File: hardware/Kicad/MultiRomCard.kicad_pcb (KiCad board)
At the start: 2 copper layers, 160 x 100 mm, 17 parts, among them P1 VC4000_Cartridge_Bus, P2 MicroSD_Breakout, U1 Arduino_UNO, U2 74HC595, U3 74HC595, U4 74HC595, U5 6264, U6 74HC245, U7 74HC245, U8 74HC245

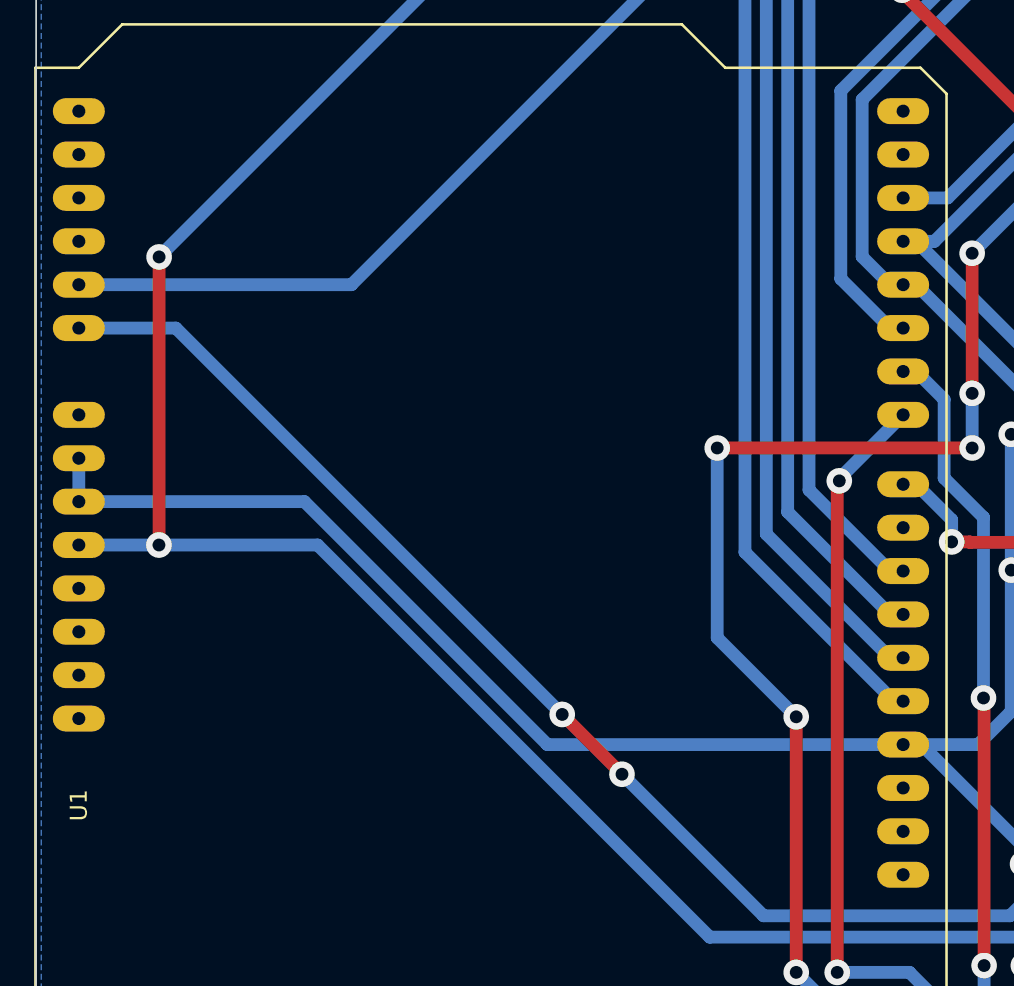
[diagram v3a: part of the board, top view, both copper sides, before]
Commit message: [PCB] Slightly bigger drill holes for Arduino footprint.
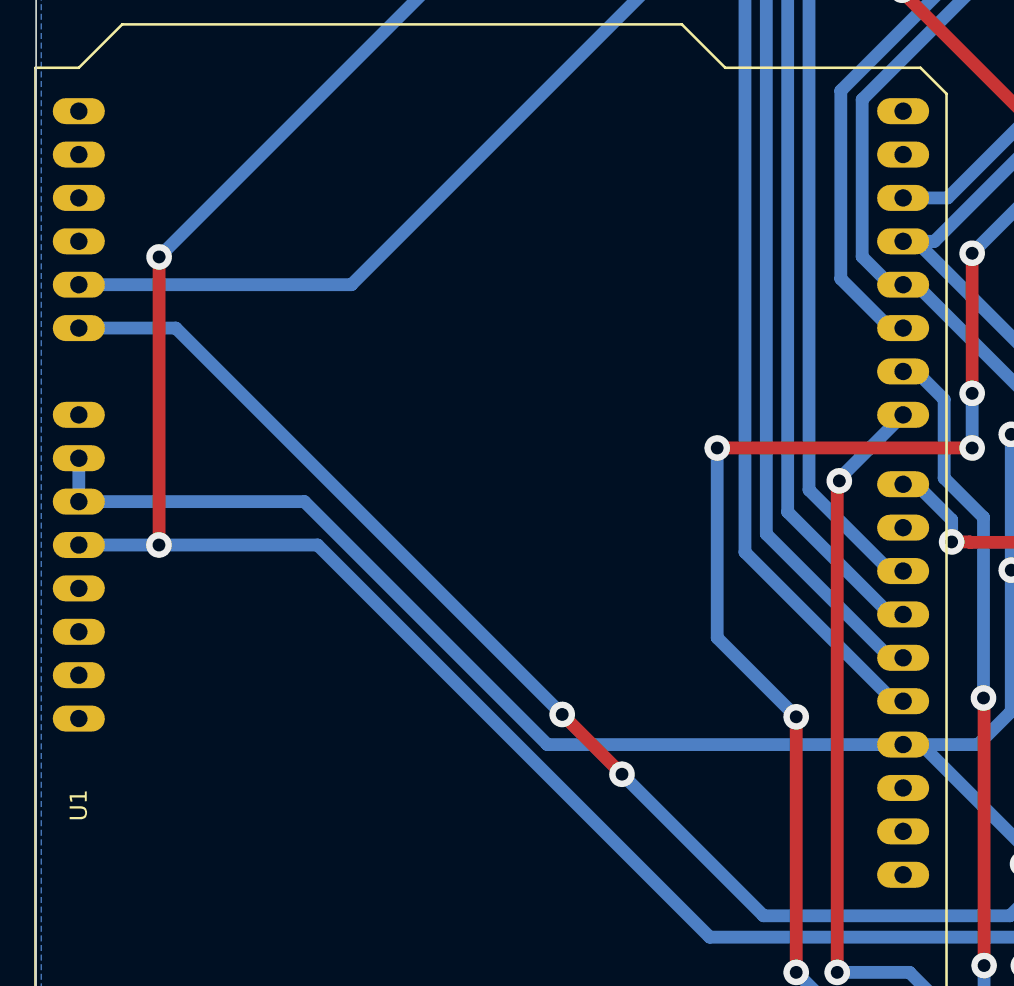
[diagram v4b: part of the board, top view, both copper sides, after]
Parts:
- U1: footprint VC4000_MultiRom:Arduino_UNO -> Arduino_UNO
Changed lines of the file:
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@@
-(kicad_pcb (version 4) (host pcbnew "(2015-06-18 BZR 5783)-product")
+(kicad_pcb (version 4) (host pcbnew "(2015-06-22 BZR 5801)-product")
   (general
     (links 133)
@@
     (uvia_drill 0.127)
   )
-  (module VC4000_MultiRom:Arduino_UNO (layer F.Cu)
+  (module Arduino_UNO (layer F.Cu)
     (at 93.9 118 270)
     (fp_text reference U1 (at 7.62 25.4 270) (layer F.SilkS)
@@
     (fp_line (start 30.48 24.765) (end 32.385 24.765) (layer F.SilkS) (width 0.15))
     (fp_line (start 30.48 27.94) (end 30.48 24.765) (layer F.SilkS) (width 0.15))
-    (pad 18 thru_hole oval (at 11.684 -22.86 270) (size 1.524 3.048) (drill 0.762) (layers *.Cu *.Mask F.SilkS))
-    (pad 17 thru_hole oval (at 9.144 -22.86 270) (size 1.524 3.048) (drill 0.762) (layers *.Cu *.Mask F.SilkS))
-    (pad 16 thru_hole oval (at 6.604 -22.86 270) (size 1.524 3.048) (drill 0.762) (layers *.Cu *.Mask F.SilkS)
+    (pad 18 thru_hole oval (at 11.684 -22.86 270) (size 1.524 3.048) (drill 1.016) (layers *.Cu *.Mask F.SilkS))
+    (pad 17 thru_hole oval (at 9.144 -22.86 270) (size 1.524 3.048) (drill 1.016) (layers *.Cu *.Mask F.SilkS))
+    (pad 16 thru_hole oval (at 6.604 -22.86 270) (size 1.524 3.048) (drill 1.016) (layers *.Cu *.Mask F.SilkS)
       (net 29 "Net-(U1-Pad16)"))
-    (pad 15 thru_hole oval (at 4.064 -22.86 270) (size 1.524 3.048) (drill 0.762) (layers *.Cu *.Mask F.SilkS)
+    (pad 15 thru_hole oval (at 4.064 -22.86 270) (size 1.524 3.048) (drill 1.016) (layers *.Cu *.Mask F.SilkS)
       (net 25 GND))
-    (pad 14 thru_hole oval (at 1.524 -22.86 270) (size 1.524 3.048) (drill 0.762) (layers *.Cu *.Mask F.SilkS)
+    (pad 14 thru_hole oval (at 1.524 -22.86 270) (size 1.524 3.048) (drill 1.016) (layers *.Cu *.Mask F.SilkS)
       (net 80 "Net-(P2-Pad1)"))
-    (pad 13 thru_hole oval (at -1.016 -22.86 270) (size 1.524 3.048) (drill 0.762) (layers *.Cu *.Mask F.SilkS)
+    (pad 13 thru_hole oval (at -1.016 -22.86 270) (size 1.524 3.048) (drill 1.016) (layers *.Cu *.Mask F.SilkS)
       (net 81 "Net-(P2-Pad2)"))
-    (pad 12 thru_hole oval (at -3.556 -22.86 270) (size 1.524 3.048) (drill 0.762) (layers *.Cu *.Mask F.SilkS)
+    (pad 12 thru_hole oval (at -3.556 -22.86 270) (size 1.524 3.048) (drill 1.016) (layers *.Cu *.Mask F.SilkS)
       (net 82 "Net-(P2-Pad3)"))
-    (pad 11 thru_hole oval (at -6.096 -22.86 270) (size 1.524 3.048) (drill 0.762) (layers *.Cu *.Mask F.SilkS)
+    (pad 11 thru_hole oval (at -6.096 -22.86 270) (size 1.524 3.048) (drill 1.016) (layers *.Cu *.Mask F.SilkS)
       (net 83 "Net-(P2-Pad4)"))
-    (pad 10 thru_hole oval (at -8.636 -22.86 270) (size 1.524 3.048) (drill 0.762) (layers *.Cu *.Mask F.SilkS)
+    (pad 10 thru_hole oval (at -8.636 -22.86 270) (size 1.524 3.048) (drill 1.016) (layers *.Cu *.Mask F.SilkS)
       (net 30 "Net-(U1-Pad10)"))
-    (pad 9 thru_hole oval (at -11.176 -22.86 270) (size 1.524 3.048) (drill 0.762) (layers *.Cu *.Mask F.SilkS)
+    (pad 9 thru_hole oval (at -11.176 -22.86 270) (size 1.524 3.048) (drill 1.016) (layers *.Cu *.Mask F.SilkS)
       (net 31 CE2SRAM))
-    (pad 8 thru_hole oval (at -15.24 -22.86 270) (size 1.524 3.048) (drill 0.762) (layers *.Cu *.Mask F.SilkS)
+    (pad 8 thru_hole oval (at -15.24 -22.86 270) (size 1.524 3.048) (drill 1.016) (layers *.Cu *.Mask F.SilkS)
       (net 32 CE1SRAM))
-    (pad 7 thru_hole oval (at -17.78 -22.86 270) (size 1.524 3.048) (drill 0.762) (layers *.Cu *.Mask F.SilkS)
+    (pad 7 thru_hole oval (at -17.78 -22.86 270) (size 1.524 3.048) (drill 1.016) (layers *.Cu *.Mask F.SilkS)
       (net 33 OEVCBUS))
-    (pad 6 thru_hole oval (at -20.32 -22.86 270) (size 1.524 3.048) (drill 0.762) (layers *.Cu *.Mask F.SilkS)
+    (pad 6 thru_hole oval (at -20.32 -22.86 270) (size 1.524 3.048) (drill 1.016) (layers *.Cu *.Mask F.SilkS)
       (net 34 "Net-(U1-Pad6)"))
-    (pad 5 thru_hole oval (at -22.86 -22.86 270) (size 1.524 3.048) (drill 0.762) (layers *.Cu *.Mask F.SilkS)
+    (pad 5 thru_hole oval (at -22.86 -22.86 270) (size 1.524 3.048) (drill 1.016) (layers *.Cu *.Mask F.SilkS)
       (net 35 "Net-(U1-Pad5)"))
-    (pad 4 thru_hole oval (at -25.4 -22.86 270) (size 1.524 3.048) (drill 0.762) (layers *.Cu *.Mask F.SilkS)
+    (pad 4 thru_hole oval (at -25.4 -22.86 270) (size 1.524 3.048) (drill 1.016) (layers *.Cu *.Mask F.SilkS)
       (net 36 "Net-(U1-Pad4)"))
-    (pad 3 thru_hole oval (at -27.94 -22.86 270) (size 1.524 3.048) (drill 0.762) (layers *.Cu *.Mask F.SilkS)
+    (pad 3 thru_hole oval (at -27.94 -22.86 270) (size 1.524 3.048) (drill 1.016) (layers *.Cu *.Mask F.SilkS)
       (net 37 WESRAM))
-    (pad 2 thru_hole oval (at -30.48 -22.86 270) (size 1.524 3.048) (drill 0.762) (layers *.Cu *.Mask F.SilkS)
+    (pad 2 thru_hole oval (at -30.48 -22.86 270) (size 1.524 3.048) (drill 1.016) (layers *.Cu *.Mask F.SilkS)
       (net 38 "Net-(U1-Pad2)"))
-    (pad 1 thru_hole oval (at -33.02 -22.86 270) (size 1.524 3.048) (drill 0.762) (layers *.Cu *.Mask F.SilkS)
+    (pad 1 thru_hole oval (at -33.02 -22.86 270) (size 1.524 3.048) (drill 1.016) (layers *.Cu *.Mask F.SilkS)
       (net 39 "Net-(U1-Pad1)"))
-    (pad 32 thru_hole oval (at -33.02 25.4 270) (size 1.524 3.048) (drill 0.762) (layers *.Cu *.Mask F.SilkS)
+    (pad 32 thru_hole oval (at -33.02 25.4 270) (size 1.524 3.048) (drill 1.016) (layers *.Cu *.Mask F.SilkS)
       (net 40 "Net-(U1-Pad32)"))
-    (pad 31 thru_hole oval (at -30.48 25.4 270) (size 1.524 3.048) (drill 0.762) (layers *.Cu *.Mask F.SilkS)
+    (pad 31 thru_hole oval (at -30.48 25.4 270) (size 1.524 3.048) (drill 1.016) (layers *.Cu *.Mask F.SilkS)
       (net 41 "Net-(U1-Pad31)"))
-    (pad 30 thru_hole oval (at -27.94 25.4 270) (size 1.524 3.048) (drill 0.762) (layers *.Cu *.Mask F.SilkS)
+    (pad 30 thru_hole oval (at -27.94 25.4 270) (size 1.524 3.048) (drill 1.016) (layers *.Cu *.Mask F.SilkS)
       (net 42 "Net-(U1-Pad30)"))
-    (pad 29 thru_hole oval (at -25.4 25.4 270) (size 1.524 3.048) (drill 0.762) (layers *.Cu *.Mask F.SilkS)
+    (pad 29 thru_hole oval (at -25.4 25.4 270) (size 1.524 3.048) (drill 1.016) (layers *.Cu *.Mask F.SilkS)
       (net 43 "Net-(U1-Pad29)"))
-    (pad 28 thru_hole oval (at -22.86 25.4 270) (size 1.524 3.048) (drill 0.762) (layers *.Cu *.Mask F.SilkS)
+    (pad 28 thru_hole oval (at -22.86 25.4 270) (size 1.524 3.048) (drill 1.016) (layers *.Cu *.Mask F.SilkS)
       (net 44 "Net-(U1-Pad28)"))
-    (pad 27 thru_hole oval (at -20.32 25.4 270) (size 1.524 3.048) (drill 0.762) (layers *.Cu *.Mask F.SilkS)
+    (pad 27 thru_hole oval (at -20.32 25.4 270) (size 1.524 3.048) (drill 1.016) (layers *.Cu *.Mask F.SilkS)
       (net 45 "Net-(U1-Pad27)"))
-    (pad 26 thru_hole oval (at -15.24 25.4 270) (size 1.524 3.048) (drill 0.762) (layers *.Cu *.Mask F.SilkS)
+    (pad 26 thru_hole oval (at -15.24 25.4 270) (size 1.524 3.048) (drill 1.016) (layers *.Cu *.Mask F.SilkS)
       (net 46 "Net-(U1-Pad26)"))
-    (pad 25 thru_hole oval (at -12.7 25.4 270) (size 1.524 3.048) (drill 0.762) (layers *.Cu *.Mask F.SilkS)
+    (pad 25 thru_hole oval (at -12.7 25.4 270) (size 1.524 3.048) (drill 1.016) (layers *.Cu *.Mask F.SilkS)
       (net 25 GND))
-    (pad 24 thru_hole oval (at -10.16 25.4 270) (size 1.524 3.048) (drill 0.762) (layers *.Cu *.Mask F.SilkS)
+    (pad 24 thru_hole oval (at -10.16 25.4 270) (size 1.524 3.048) (drill 1.016) (layers *.Cu *.Mask F.SilkS)
       (net 25 GND))
-    (pad 23 thru_hole oval (at -7.62 25.4 270) (size 1.524 3.048) (drill 0.762) (layers *.Cu *.Mask F.SilkS)
+    (pad 23 thru_hole oval (at -7.62 25.4 270) (size 1.524 3.048) (drill 1.016) (layers *.Cu *.Mask F.SilkS)
       (net 13 VCC))
-    (pad 22 thru_hole oval (at -5.08 25.4 270) (size 1.524 3.048) (drill 0.762) (layers *.Cu *.Mask F.SilkS)
+    (pad 22 thru_hole oval (at -5.08 25.4 270) (size 1.524 3.048) (drill 1.016) (layers *.Cu *.Mask F.SilkS)
       (net 47 "Net-(U1-Pad22)"))
-    (pad 21 thru_hole oval (at -2.54 25.4 270) (size 1.524 3.048) (drill 0.762) (layers *.Cu *.Mask F.SilkS)
+    (pad 21 thru_hole oval (at -2.54 25.4 270) (size 1.524 3.048) (drill 1.016) (layers *.Cu *.Mask F.SilkS)
       (net 48 "Net-(U1-Pad21)"))
-    (pad 20 thru_hole oval (at 0 25.4 270) (size 1.524 3.048) (drill 0.762) (layers *.Cu *.Mask F.SilkS)
+    (pad 20 thru_hole oval (at 0 25.4 270) (size 1.524 3.048) (drill 1.016) (layers *.Cu *.Mask F.SilkS)
       (net 49 "Net-(U1-Pad20)"))
-    (pad 19 thru_hole oval (at 2.54 25.4 270) (size 1.524 3.048) (drill 0.762) (layers *.Cu *.Mask F.SilkS))
+    (pad 19 thru_hole oval (at 2.54 25.4 270) (size 1.524 3.048) (drill 1.016) (layers *.Cu *.Mask F.SilkS))
   )
   (module Housings_DIP:DIP-16__300_ELL (layer F.Cu)

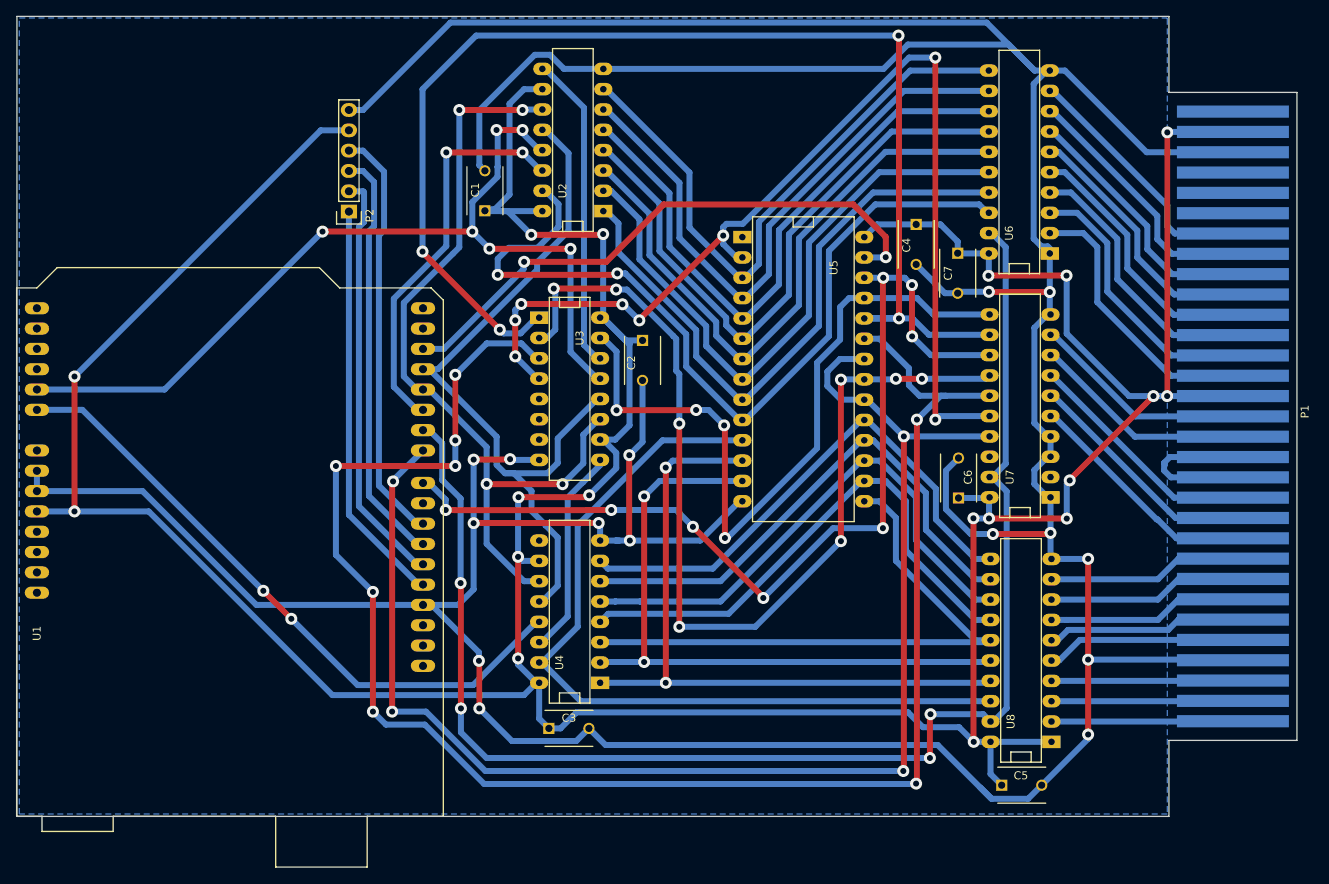
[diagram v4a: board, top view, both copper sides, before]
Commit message: [SCH/PCB] Replace Arduino UNO by Arduino Nano
- TODO: Shrink board outlines to account for smaller Arduino board.
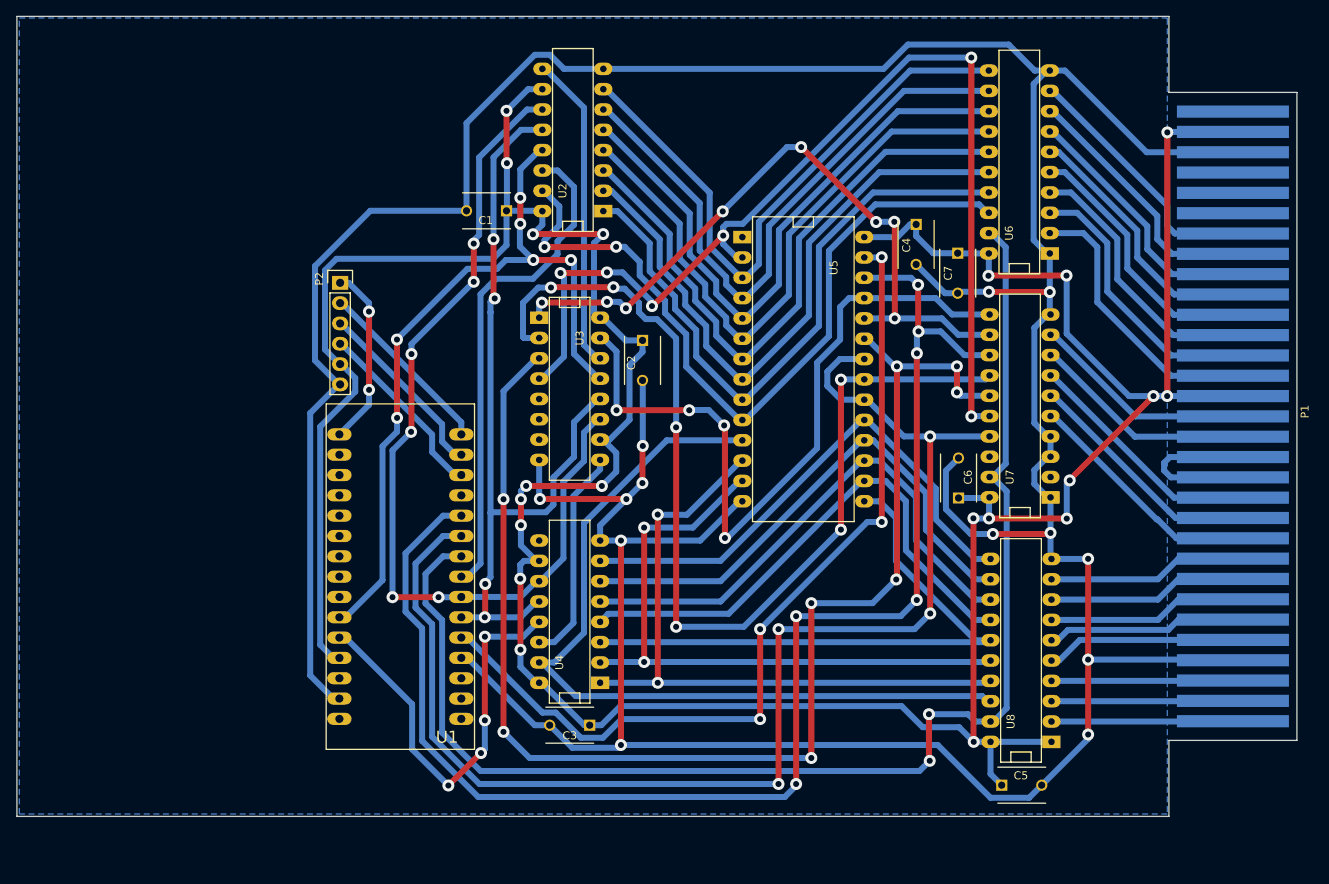
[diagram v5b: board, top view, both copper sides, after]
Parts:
- U1: value Arduino_UNO -> Arduino_Nano; footprint Arduino_UNO -> VC4000_MultiRom:Arduino_Nano
- moved U1 33.2 mm to (121.5, 136.3), turned to 180 degrees
- moved P2 8.97 mm to (106.4, 81.8), turned to 0 degrees
- moved C3 5.12 mm to (137.6, 137.1), turned to 180 degrees
- moved C1 2.70 mm to (127.2, 72.8), turned to 180 degrees
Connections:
- U1 pad 10: Net-(U1-Pad10) -> CE1SRAM
- U1 pad 11: Net-(P2-Pad4) -> CE2SRAM
- U1 pad 12: Net-(P2-Pad3) -> Net-(U1-Pad12)
- U1 pad 13: Net-(P2-Pad2) -> Net-(P2-Pad4)
- U1 pad 14: Net-(P2-Pad1) -> Net-(P2-Pad3)
- U1 pad 15: GND -> Net-(P2-Pad2)
- U1 pad 16: Net-(U1-Pad16) -> Net-(P2-Pad1)
- U1 pad 17: (no net) -> Net-(U1-Pad17)
- U1 pad 18: (no net) -> Net-(U1-Pad18)
- U1 pad 19: (no net) -> Net-(U1-Pad19)
- U1 pad 23: VCC -> Net-(U1-Pad23)
- U1 pad 24: GND -> Net-(U1-Pad24)
- U1 pad 25: GND -> Net-(U1-Pad25)
- U1 pad 27: Net-(U1-Pad27) -> VCC
- U1 pad 29: Net-(U1-Pad29) -> GND
- U1 pad 3: WESRAM -> Net-(U1-Pad3)
- U1 pad 4: Net-(U1-Pad4) -> GND
- U1 pad 5: Net-(U1-Pad5) -> WESRAM
- U1 pad 7: OEVCBUS -> Net-(U1-Pad7)
- U1 pad 8: CE1SRAM -> Net-(U1-Pad8)
- U1 pad 9: CE2SRAM -> OEVCBUS
- U2 pad 11: Net-(U1-Pad5) -> Net-(U1-Pad7)
- U2 pad 12: Net-(U1-Pad4) -> Net-(U1-Pad6)
- U2 pad 13: Net-(U1-Pad28) -> Net-(U1-Pad25)
- U2 pad 14: Net-(U1-Pad6) -> Net-(U1-Pad8)
- U3 pad 11: Net-(U1-Pad5) -> Net-(U1-Pad7)
- U3 pad 12: Net-(U1-Pad4) -> Net-(U1-Pad6)
- U3 pad 13: Net-(U1-Pad28) -> Net-(U1-Pad25)
- U4 pad 11: Net-(U1-Pad5) -> Net-(U1-Pad7)
- U4 pad 12: Net-(U1-Pad4) -> Net-(U1-Pad6)
- U4 pad 13: Net-(U1-Pad27) -> Net-(U1-Pad26)
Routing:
- net Net-(U1-Pad28): track 114.8 -> 0.00 mm, vias 6 -> 0
- net Net-(U1-Pad7): track 0.00 -> 112.7 mm, vias 0 -> 6
- net Net-(U1-Pad5): track 100.9 -> 0.00 mm, vias 4 -> 0
- net Net-(U1-Pad25): track 0.00 -> 96.3 mm, vias 0 -> 6
- net Net-(U1-Pad4): track 96.1 -> 0.00 mm
- net GND: track 609.5 -> 524.4 mm, vias 15 -> 13
- net Net-(U1-Pad27): track 80.3 -> 0.00 mm, vias 2 -> 0
- net /A9: track 158.5 -> 87.5 mm, vias 4 -> 8
- net VCC: track 507.1 -> 440.6 mm, vias 18 -> 20
- net Net-(U1-Pad8): track 0.00 -> 62.5 mm
- net CE2SRAM: track 122.7 -> 177.3 mm, vias 8 -> 6
- net Net-(U1-Pad26): track 0.00 -> 52.6 mm, vias 0 -> 4
- net Net-(U1-Pad6): track 49.8 -> 100.4 mm, vias 2 -> 4
- net /A11: track 213.7 -> 167.4 mm
- net WESRAM: track 72.8 -> 110.8 mm, vias 2 -> 4
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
